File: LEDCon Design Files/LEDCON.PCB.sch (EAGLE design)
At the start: 23 parts

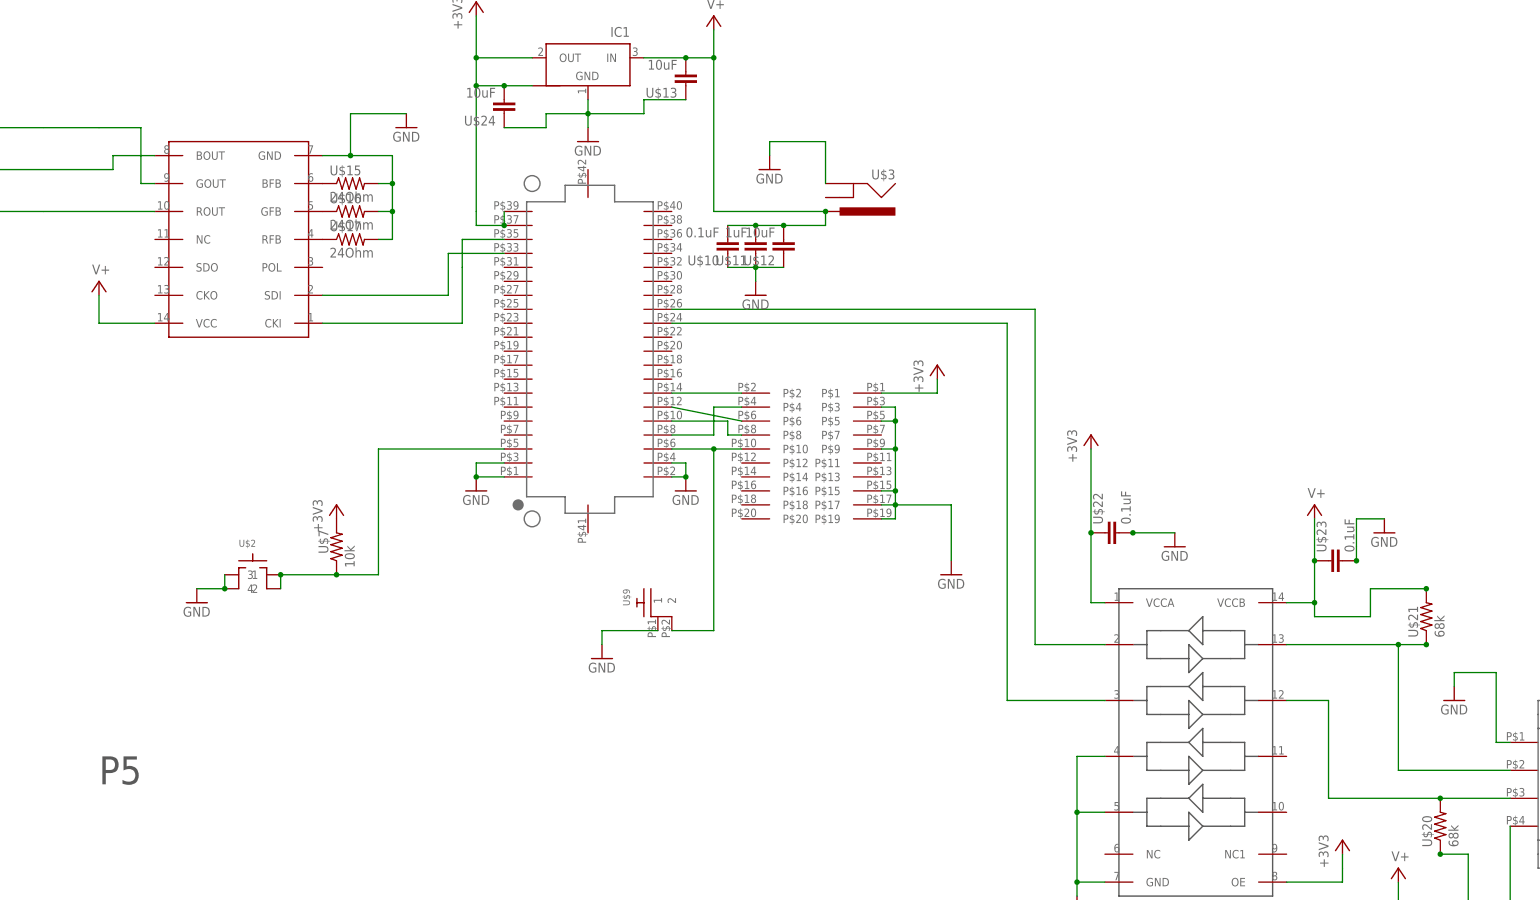
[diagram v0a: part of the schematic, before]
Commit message: LEDCON.PCB.v1.0 pre-release
Pending checklist processing.
Fixed reset switch orientation, added planes, silk screen labelling,
added all part numbers, exported production files, added BOM, ECO and
FAB notes.
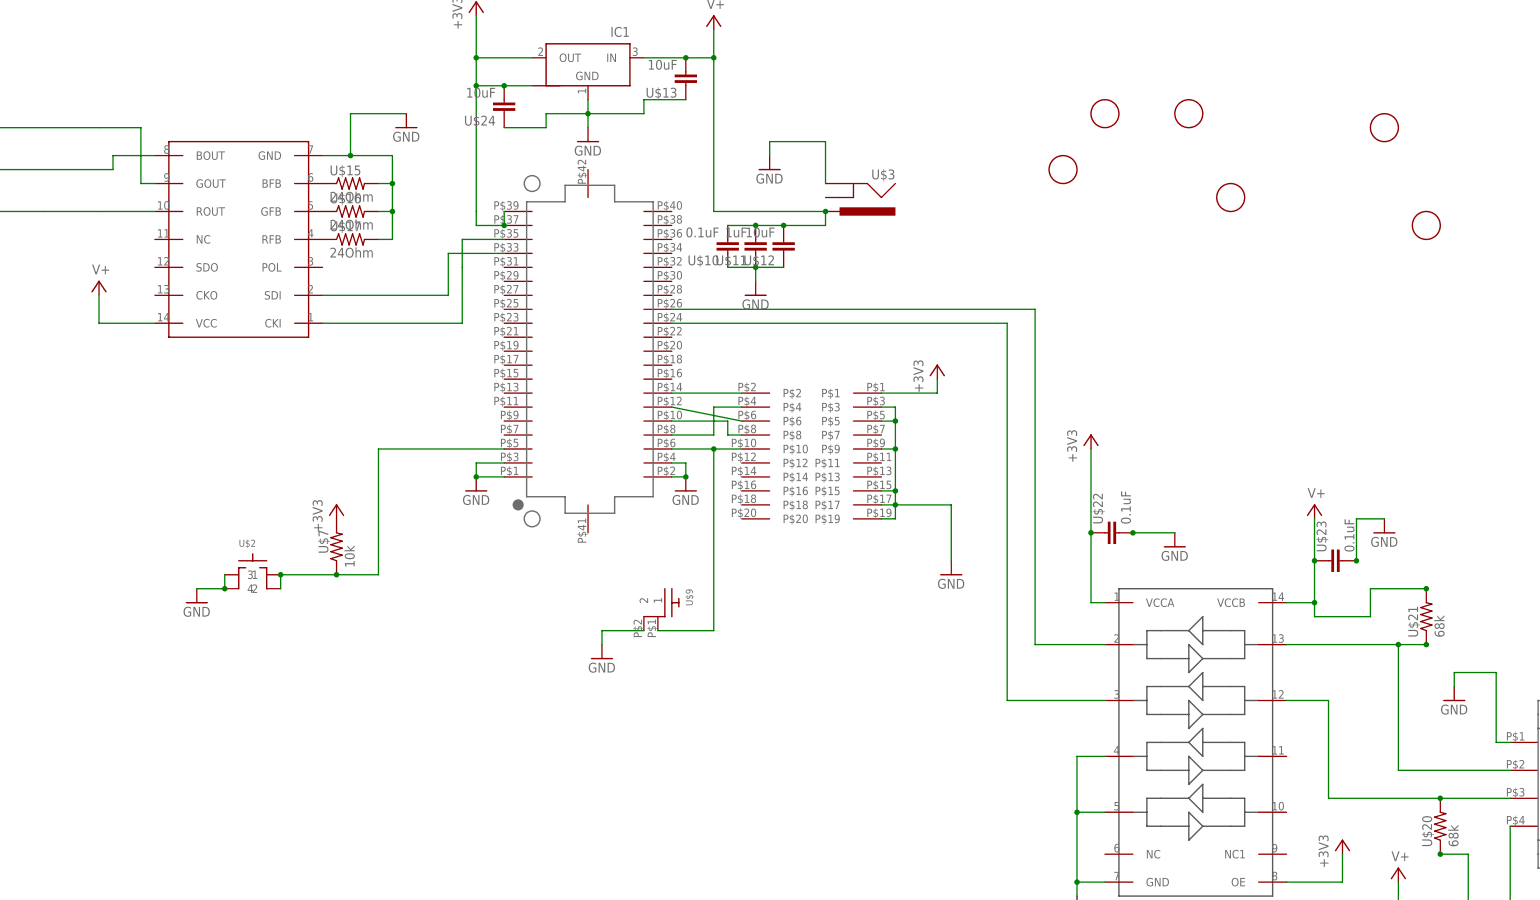
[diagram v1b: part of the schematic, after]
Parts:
- added U$14, U$18, U$25, U$26, U$27, U$28: FIDUCIAL, adafruit:FIDUCIAL
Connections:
- net GND: now also U$9.2; no longer U$9.1
- net N$3: now also U$9.1; no longer U$9.2
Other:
- note removed: "P5"
- moved on the sheet: U$9

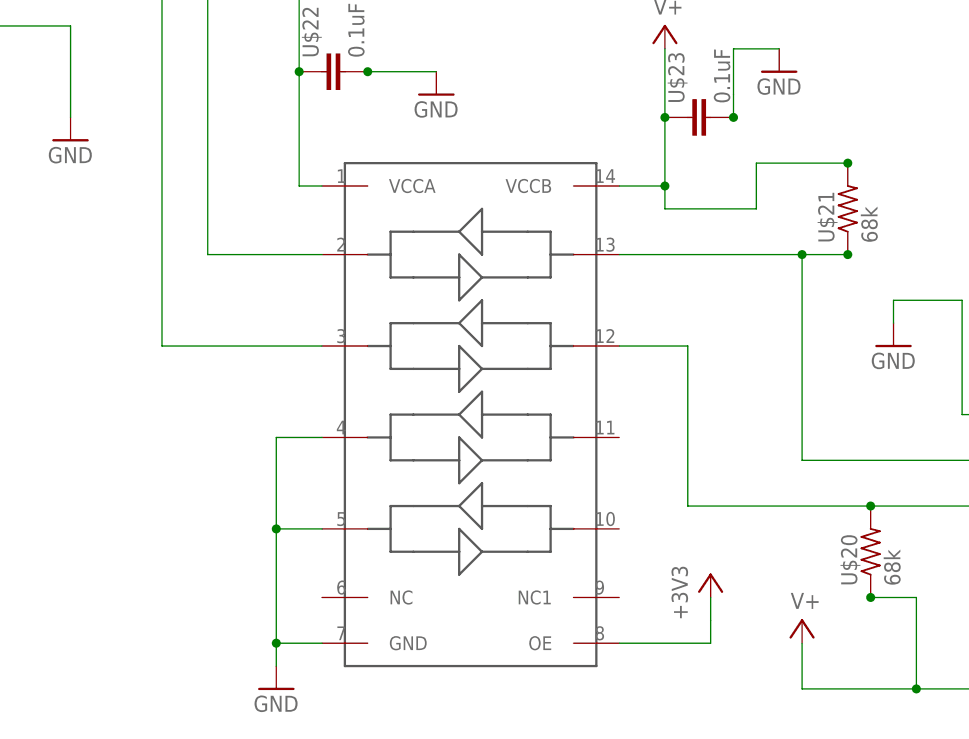
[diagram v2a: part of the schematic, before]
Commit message: Removed level shifter (no layout change)
Also test commit for branch.
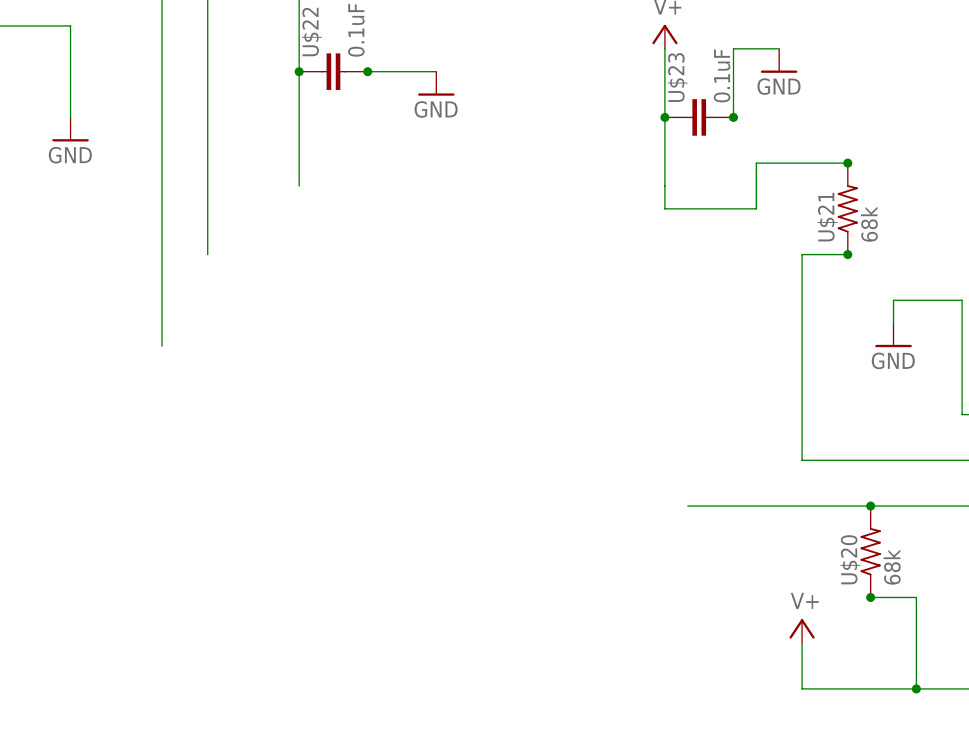
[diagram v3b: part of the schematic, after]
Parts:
- removed U$6: TXB0104, texas:TXB0104
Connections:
- net +3V3: no longer U$6.OE, U$6.VCCA
- net CLK_5V: no longer U$6.P$12
- net DAT_5V: no longer U$6.P$13
- net GND: no longer U$6.GND, U$6.P$4, U$6.P$5
- net N$1: no longer U$6.P$2
- net N$2: no longer U$6.P$3
- net V+: no longer U$6.VCCB
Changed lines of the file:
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@@
 <?xml version="1.0" encoding="utf-8"?>
 <!DOCTYPE eagle SYSTEM "eagle.dtd">
-<eagle version="6.5.0">
+<eagle version="6.6.0">
 <drawing>
 <settings>
@@
 <part name="+3V1" library="supply1" deviceset="+3V3" device=""/>
 <part name="GND3" library="supply1" deviceset="GND" device=""/>
-<part name="U$6" library="texas" deviceset="TXB0104" device="" value="">
-<attribute name="MFGN" value="Texas Instruments"/>
-</part>
 <part name="GND4" library="supply1" deviceset="GND" device=""/>
 <part name="SUPPLY1" library="supply2" deviceset="V+" device=""/>
@@
 <part name="+3V2" library="supply1" deviceset="+3V3" device=""/>
 <part name="SUPPLY3" library="supply2" deviceset="V+" device=""/>
-<part name="GND5" library="supply1" deviceset="GND" device=""/>
-<part name="+3V4" library="supply1" deviceset="+3V3" device=""/>
 <part name="GND6" library="supply1" deviceset="GND" device=""/>
 <part name="U$8" library="GW-devices" deviceset="WS2801" device="" value=""/>
@@
 <instance part="+3V1" gate="G$1" x="-10.16" y="45.72"/>
 <instance part="GND3" gate="1" x="43.18" y="15.24"/>
-<instance part="U$6" gate="G$1" x="121.92" y="-96.52">
-<attribute name="MFGN" x="121.92" y="-96.52" size="1.778" layer="96" display="off"/>
-<attribute name="MFGP" x="121.92" y="-96.52" size="1.778" layer="96" display="off"/>
-</instance>
 <instance part="GND4" gate="1" x="167.64" y="-81.28"/>
 <instance part="SUPPLY1" gate="1" x="33.02" y="43.18"/>
@@
 <instance part="+3V2" gate="G$1" x="101.6" y="-33.02"/>
 <instance part="SUPPLY3" gate="1" x="142.24" y="-45.72"/>
-<instance part="GND5" gate="1" x="99.06" y="-119.38"/>
-<instance part="+3V4" gate="G$1" x="147.32" y="-106.68"/>
 <instance part="GND6" gate="1" x="-60.96" y="-63.5"/>
 <instance part="U$8" gate="G$1" x="-55.88" y="2.54" rot="R180"/>
@@
 <wire x1="175.26" y1="-76.2" x2="167.64" y2="-76.2" width="0.1524" layer="91"/>
 <wire x1="167.64" y1="-76.2" x2="167.64" y2="-78.74" width="0.1524" layer="91"/>
-</segment>
-<segment>
-<pinref part="U$6" gate="G$1" pin="GND"/>
-<pinref part="GND5" gate="1" pin="GND"/>
-<wire x1="104.14" y1="-114.3" x2="99.06" y2="-114.3" width="0.1524" layer="91"/>
-<wire x1="99.06" y1="-114.3" x2="99.06" y2="-116.84" width="0.1524" layer="91"/>
-<pinref part="U$6" gate="G$1" pin="P$5"/>
-<wire x1="104.14" y1="-101.6" x2="99.06" y2="-101.6" width="0.1524" layer="91"/>
-<wire x1="99.06" y1="-101.6" x2="99.06" y2="-114.3" width="0.1524" layer="91"/>
-<pinref part="U$6" gate="G$1" pin="P$4"/>
-<wire x1="104.14" y1="-91.44" x2="99.06" y2="-91.44" width="0.1524" layer="91"/>
-<wire x1="99.06" y1="-91.44" x2="99.06" y2="-101.6" width="0.1524" layer="91"/>
-<junction x="99.06" y="-101.6"/>
-<junction x="99.06" y="-114.3"/>
 </segment>
 <segment>
@@
 </segment>
 <segment>
-<pinref part="U$6" gate="G$1" pin="VCCA"/>
 <pinref part="+3V2" gate="G$1" pin="+3V3"/>
-<wire x1="104.14" y1="-63.5" x2="101.6" y2="-63.5" width="0.1524" layer="91"/>
 <wire x1="101.6" y1="-63.5" x2="101.6" y2="-50.8" width="0.1524" layer="91"/>
 <pinref part="U$22" gate="G$1" pin="1"/>
 <junction x="101.6" y="-50.8"/>
 <wire x1="101.6" y1="-50.8" x2="101.6" y2="-35.56" width="0.1524" layer="91"/>
-</segment>
-<segment>
-<pinref part="+3V4" gate="G$1" pin="+3V3"/>
-<wire x1="147.32" y1="-109.22" x2="147.32" y2="-111.76" width="0.1524" layer="91"/>
-<pinref part="U$6" gate="G$1" pin="OE"/>
-<wire x1="147.32" y1="-111.76" x2="147.32" y2="-114.3" width="0.1524" layer="91"/>
-<wire x1="147.32" y1="-114.3" x2="137.16" y2="-114.3" width="0.1524" layer="91"/>
 </segment>
 <segment>
@@
 </segment>
 <segment>
-<pinref part="U$6" gate="G$1" pin="VCCB"/>
 <pinref part="SUPPLY3" gate="1" pin="V+"/>
-<wire x1="137.16" y1="-63.5" x2="142.24" y2="-63.5" width="0.1524" layer="91"/>
 <wire x1="142.24" y1="-63.5" x2="142.24" y2="-55.88" width="0.1524" layer="91"/>
 <wire x1="142.24" y1="-55.88" x2="142.24" y2="-48.26" width="0.1524" layer="91"/>
@@
 <junction x="142.24" y="-55.88"/>
 <junction x="162.56" y="-60.96"/>
-<junction x="142.24" y="-63.5"/>
 </segment>
 <segment>
@@
 <net name="DAT_5V" class="0">
 <segment>
-<pinref part="U$6" gate="G$1" pin="P$13"/>
-<wire x1="137.16" y1="-71.12" x2="157.48" y2="-71.12" width="0.1524" layer="91"/>
 <wire x1="157.48" y1="-71.12" x2="157.48" y2="-93.98" width="0.1524" layer="91"/>
 <pinref part="U$1" gate="G$1" pin="P$2"/>
@@
 <pinref part="U$21" gate="G$1" pin="1"/>
 <wire x1="157.48" y1="-71.12" x2="162.56" y2="-71.12" width="0.1524" layer="91"/>
-<junction x="157.48" y="-71.12"/>
 <junction x="162.56" y="-71.12"/>
 </segment>
@@
 <wire x1="177.8" y1="-99.06" x2="165.1" y2="-99.06" width="0.1524" layer="91"/>
 <wire x1="165.1" y1="-99.06" x2="144.78" y2="-99.06" width="0.1524" layer="91"/>
-<wire x1="144.78" y1="-99.06" x2="144.78" y2="-81.28" width="0.1524" layer="91"/>
-<pinref part="U$6" gate="G$1" pin="P$12"/>
-<wire x1="144.78" y1="-81.28" x2="137.16" y2="-81.28" width="0.1524" layer="91"/>
 <pinref part="U$20" gate="G$1" pin="2"/>
 <junction x="165.1" y="-99.06"/>
@@
 <net name="N$1" class="0">
 <segment>
-<pinref part="U$6" gate="G$1" pin="P$2"/>
 <wire x1="91.44" y1="-10.16" x2="91.44" y2="-71.12" width="0.1524" layer="91"/>
-<wire x1="91.44" y1="-71.12" x2="104.14" y2="-71.12" width="0.1524" layer="91"/>
 <pinref part="U$4" gate="G$1" pin="PTC6/LLWU_P10/CMP0_IN0/SPI0_SOUT/PDB0_EXTRG/I2S0_RX_BCLK/I2S0_MCLK"/>
 <wire x1="91.44" y1="-10.16" x2="25.4" y2="-10.16" width="0.1524" layer="91"/>
@@
 <net name="N$2" class="0">
 <segment>
-<pinref part="U$6" gate="G$1" pin="P$3"/>
 <wire x1="86.36" y1="-12.7" x2="86.36" y2="-81.28" width="0.1524" layer="91"/>
-<wire x1="86.36" y1="-81.28" x2="104.14" y2="-81.28" width="0.1524" layer="91"/>
 <pinref part="U$4" gate="G$1" pin="PTC5/LLWU_P8/SPI0_PCS0/UART1_TX/FTM0_CH3/CMP1_OUT"/>
 <wire x1="86.36" y1="-12.7" x2="25.4" y2="-12.7" width="0.1524" layer="91"/>

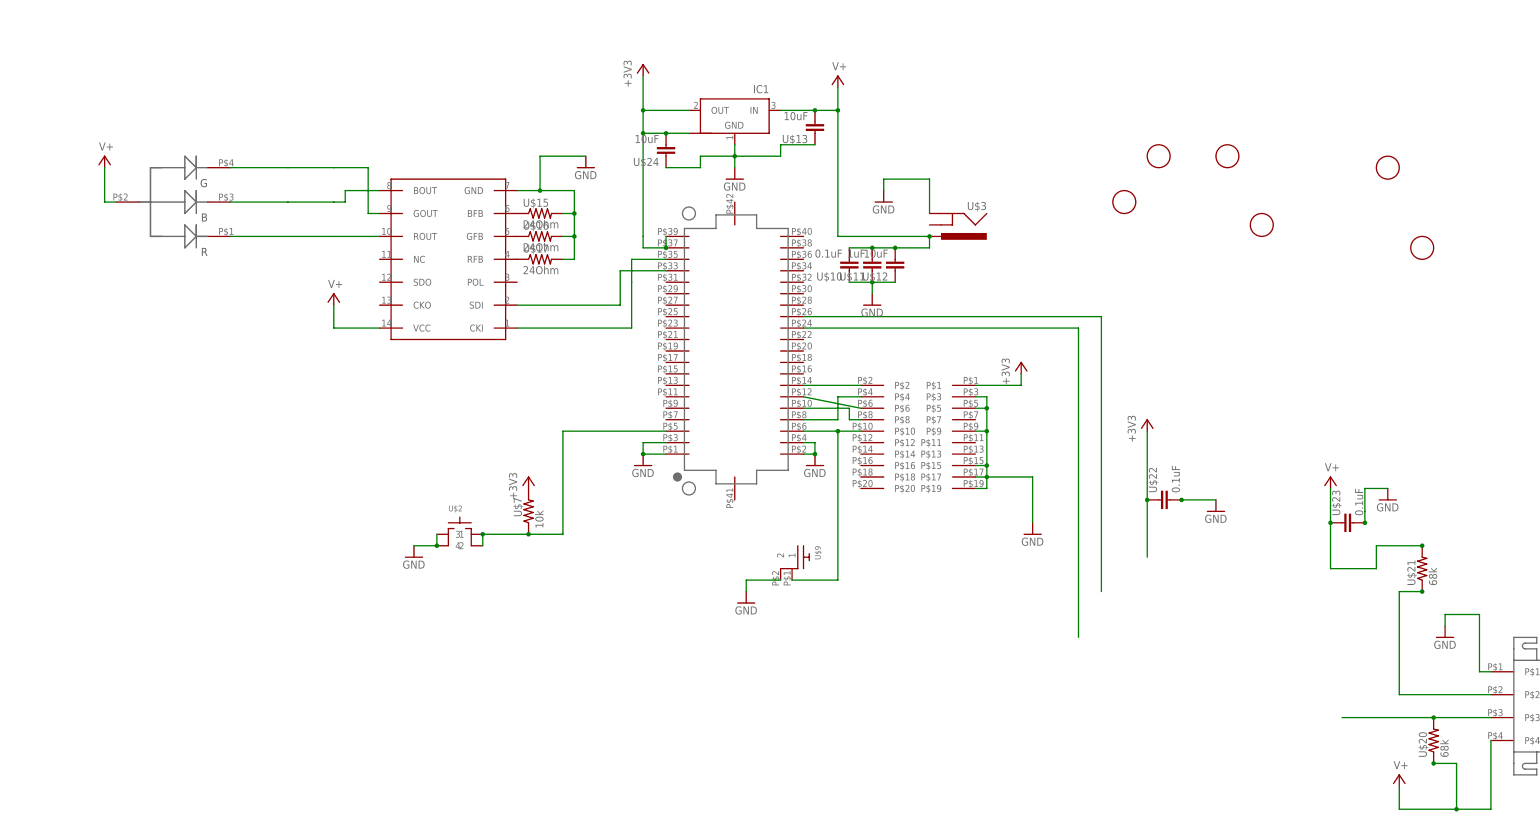
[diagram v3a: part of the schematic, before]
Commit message: 24V V1
LED still there (need to blast off). Added 24V reg + capacitors
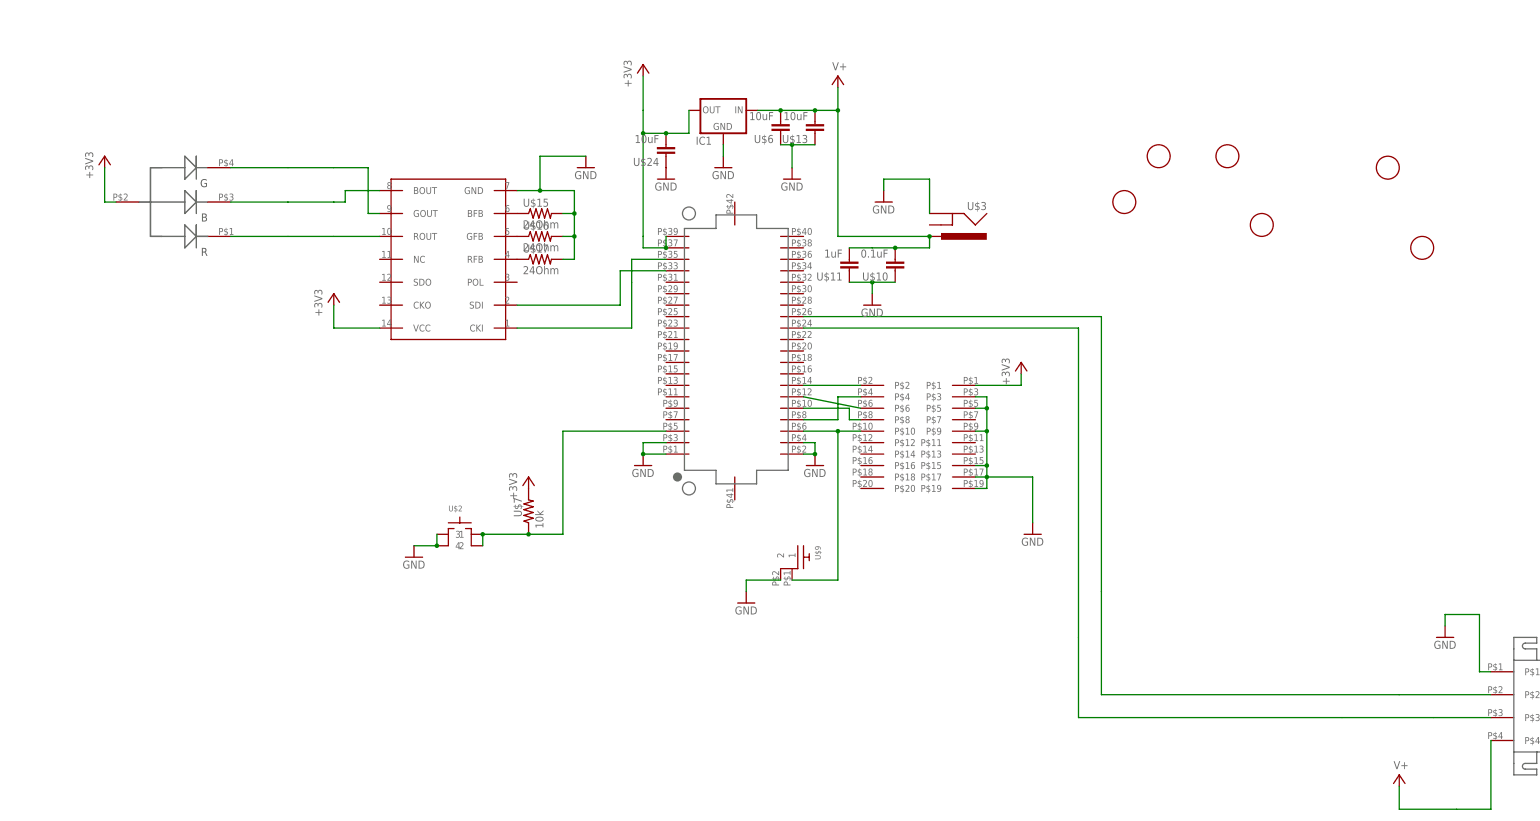
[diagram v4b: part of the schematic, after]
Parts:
- removed U$12: 10uF, GW-devices:RF-C0805
- removed U$20, U$21: 68k, GW-devices:RF-R0805
- removed U$22, U$23: 0.1uF, GW-devices:RF-C0805
- added U$6: 10uF, GW-devices:RF-C1210
- IC1: device KW2:NCP1117ST33T3G_1 -> SparkFun:V_REG_78XX; MFGN OnSemi -> (none); MFGP NCP1117ST33T3G -> (none)
- U$10: MFGN TDK -> Murata; MFGP C2012X5R1H104K085AA -> GRM21BR71H104MA01L
- U$11: MFGN TDK -> Murata; MFGP C2012X5R1E105K125AA -> GRJ21BR71H105KE01L
- U$13: device GW-devices:RF-C0805 -> GW-devices:RF-C1210; MFGP GRM219R61E106KA12D -> GRM32ER71H106KA12L
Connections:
- removed net N$1: U$4.PTC6/LLWU_P10/CMP0_IN0/SPI0_SOUT/PDB0_EXTRG/I2S0_RX_BCLK/I2S0_MCLK
- removed net N$2: U$4.PTC5/LLWU_P8/SPI0_PCS0/UART1_TX/FTM0_CH3/CMP1_OUT
- net +3V3: now also U$5.ANODE, U$8.VCC; no longer IC1.OUT1, U$22.1
- net CLK_5V: now also U$4.PTC5/LLWU_P8/SPI0_PCS0/UART1_TX/FTM0_CH3/CMP1_OUT; no longer U$20.2
- net DAT_5V: now also U$4.PTC6/LLWU_P10/CMP0_IN0/SPI0_SOUT/PDB0_EXTRG/I2S0_RX_BCLK/I2S0_MCLK; no longer U$21.1
- net GND: now also U$6.1; no longer U$12.1, U$22.2, U$23.2
- net V+: now also U$6.2; no longer U$12.2, U$20.1, U$21.2, U$23.1, U$5.ANODE, U$8.VCC
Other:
- moved on the sheet: U$10, U$11
